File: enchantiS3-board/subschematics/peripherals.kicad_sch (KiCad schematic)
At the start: 16 parts

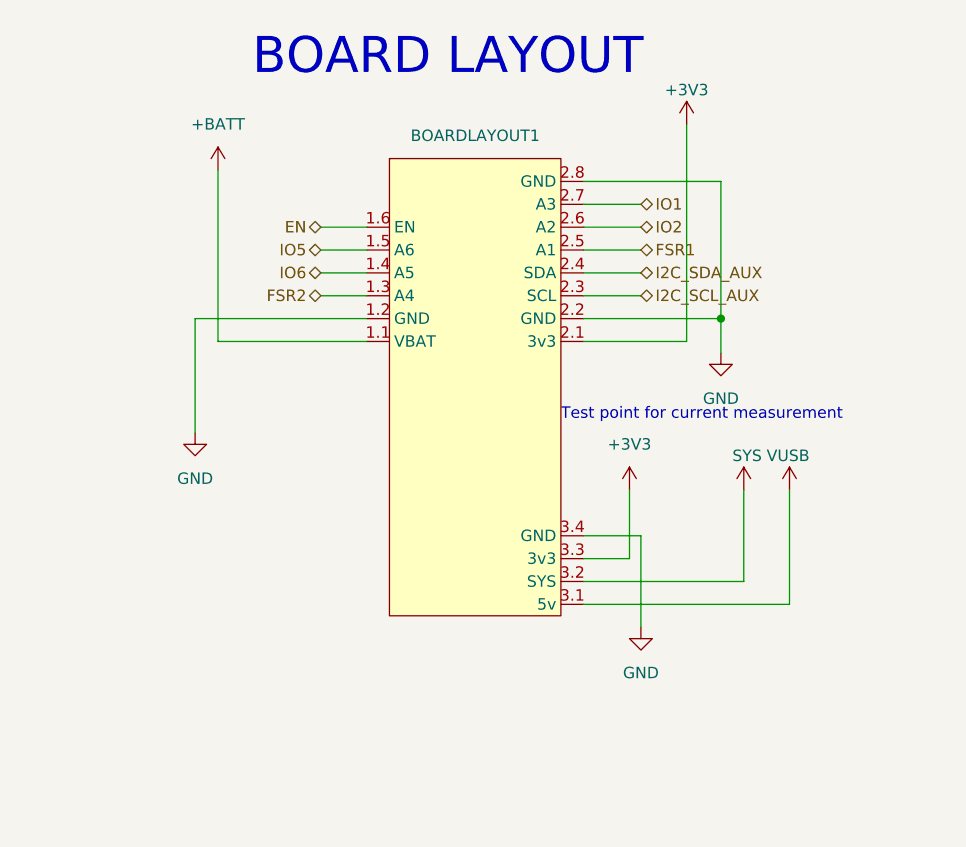
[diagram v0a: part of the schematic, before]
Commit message: Moved all subschematics to a folder
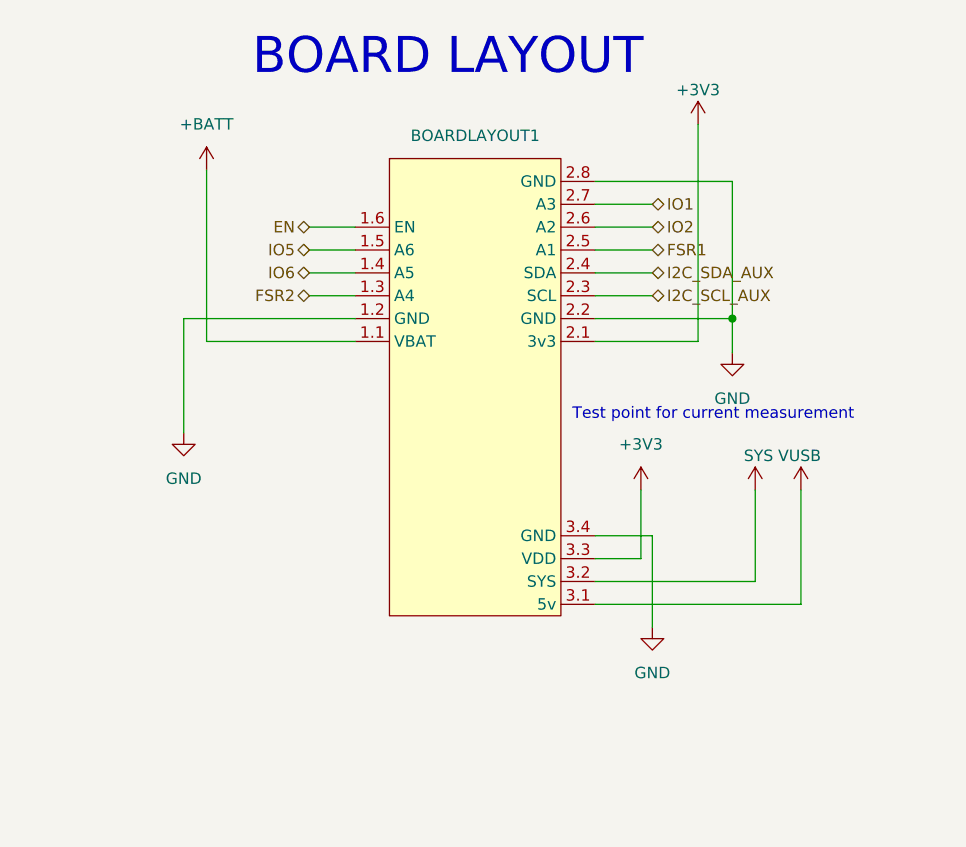
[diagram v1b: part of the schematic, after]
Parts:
- BOARDLAYOUT1: footprint ENCHANTI_enchanti-board-symbols:enchantiS3-layout -> ENCHANTI_enchanti-board-symbols:enchantiC5-layout; symbol ENCHANTI_enchanti_board_symbols:board-layout -> ENCHANTI_enchanti_board_symbols:enchantiC5-layout

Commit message: Added circuit for magnetometer, added circuit for canfd transceiver, updated circuit for USB connector
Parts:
- added C14, C7: 0.1uF, Capacitor_SMD:C_0402_1005Metric, symbol Device:C
- added C6: 1uF, Capacitor_SMD:C_0402_1005Metric, symbol Device:C
- added D2: NUP2105L, Package_TO_SOT_SMD:SOT-23, symbol Power_Protection:NUP2105L
- added H3: MountingHole, MountingHole:MountingHole_3.2mm_M3_DIN965, symbol Mechanical:MountingHole
- added R16: 120, Resistor_SMD:R_0402_1005Metric, symbol Device:R_US
- added TOUCH2: JST-SH-1x04 1.0mm, ENCHANTI_connectors:JST_SMD_1.0mm-4_Vertical, symbol ENCHANTI_connectors:QWIIC-CONNECTOR
- added U7: TCAN3413DDFR, ENCHANTI_transceivers:TSOT-23-8_DDF_TEX, symbol ENCHANTI_transceivers:TCAN3413DDFR
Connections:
- net +3V3: now also TOUCH2.2 (3v3)
- net GND: now also C14.2, C6.2, C7.2, D2.3 (A), TOUCH2.1 (GND), U7.2 (GND)
- new net: TOUCH2.NC1 (NC), TOUCH2.NC2 (NC)
- new net CAN_H: D2.2 (K), R16.2, TOUCH2.3 (SDA), U7.7 (CANH)
- new net CAN_L: D2.1 (K), R16.1, TOUCH2.4 (SCL), U7.6 (CANL)
- new net FDCAN_RX: U7.4 (RXD)
- new net FDCAN_TX: U7.1 (TXD)
- new net VCC: C6.1, C7.1, U7.3 (VCC)
- new net VIO: C14.1, U7.5 (VIO)
- new net ~{CAN_EN}: U7.8 (STB)
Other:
- note added: "Bypass Capacitors"
- note added: "CAN TRANSCEIVER"
- note added: "CANFD 4 pin connector"
- note added: "ESD Protection"
- moved on the sheet: H1, H2, LED1, LED2, R10, R7, R8, R9, TOUCH1

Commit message: Added can transceiver circuit, finished routing power traces
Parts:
- removed ANG2: CONN HEADER SMD 2POS 1MM, ENCHANTI_connectors:Molex_Pico-Clasp_2pin_Vertical, symbol ENCHANTI_connectors:PicoClasp_2pin
- removed TOUCH1: JST-SH-1x04 1.0mm, ENCHANTI_connectors:JST_SMD_1.0mm-4_Vertical, symbol ENCHANTI_connectors:QWIIC-CONNECTOR
- added J2: Conn_01x06, PCM_SparkFun-Connector:JST_1x06_P1.0mm_Vertical_SMD, symbol PCM_SparkFun-Connector:Conn_01x06_JST_P1.0mm_Vertical_SMD
- added J3: Qwiic_Connector, PCM_SparkFun-Connector:JST_1x04_P1.0mm_Horizontal_SMD, symbol ENCHANTI_connectors:QWIIC-CONNECTOR_RA
- ANG1, ANG3, R1, R2: now not fitted; now left out of the parts list
- BOARDLAYOUT1: footprint ENCHANTI_enchanti-board-symbols:enchantiC5-layout -> ENCHANTI_enchanti-board-symbols:enchantis31-layout; symbol ENCHANTI_enchanti_board_symbols:enchantiC5-layout -> ENCHANTI_enchanti_board_symbols:s31-board-layout
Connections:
- net VCC is gone; now on net +3V3: C6.1, C7.1, U7.3 (VCC)
- net VIO is gone; now on net +3V3: C14.1, U7.5 (VIO)
- net +3V3: now also J2.2 (Pin_2), J3.2 (3v3)
- net GND: now also J2.1 (Pin_1), J3.1 (GND)
- net I2C_SCL_AUX: now also J3.4 (SCL)
- net I2C_SDA_AUX: now also J3.3 (SDA)
- net PWR_BUTTON: now also J2.3 (Pin_3)
- new net: J3.NC1 (NC), J3.NC2 (NC)
